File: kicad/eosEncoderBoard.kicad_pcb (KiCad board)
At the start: 2 copper layers, 235 x 45 mm, 72 parts, among them J1 USB_C_Receptacle_USB2.0_16P, J2 DEBUG, J3 EXTRA, SW1 RotaryEncoder, SW10 SHUTTER, SW11 SW_Push, SW2 RotaryEncoder, SW3 RotaryEncoder, SW4 RotaryEncoder, SW5 INTENS, SW6 FORM, SW7 FOCUS, SW8 IMAGE, SW9 COLOR, U1 STM32L072CZT6TR, U2 PCA9548ADB, U3 TPS62A01DRLR, Y1 OSC16M-3.3I/S3T

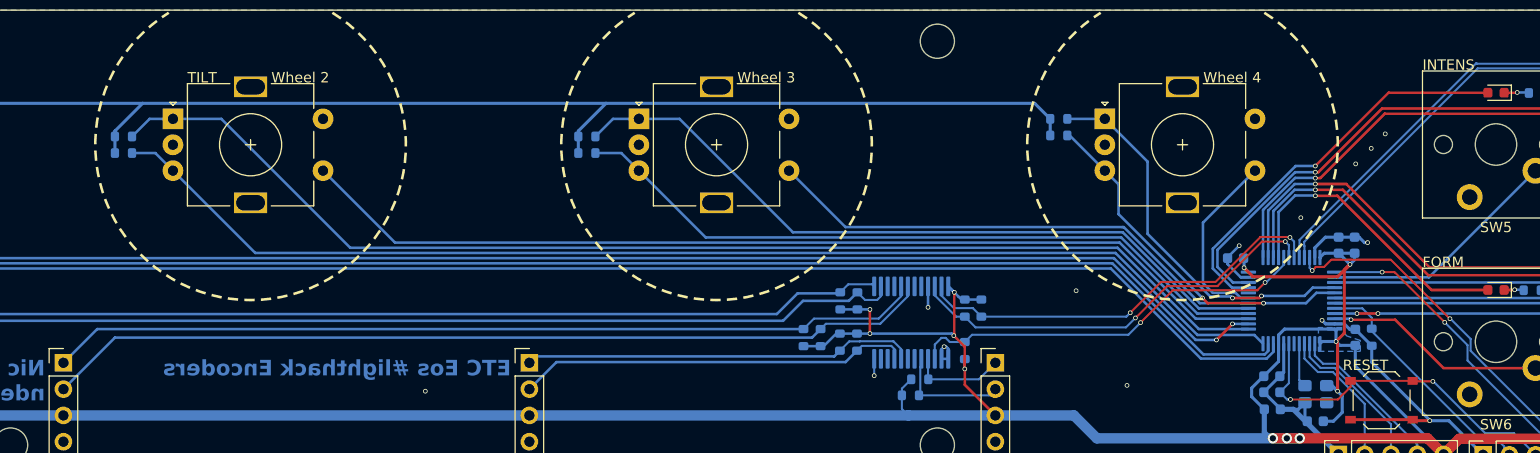
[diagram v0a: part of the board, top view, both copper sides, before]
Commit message: some minor include optimizations, going to stick with adafruit display library
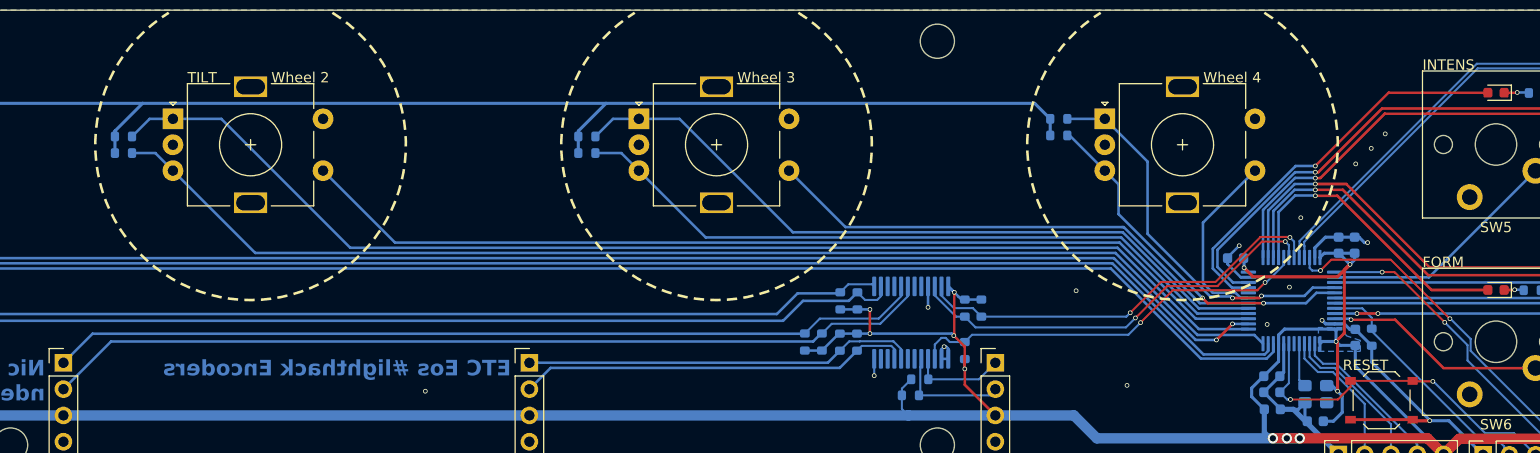
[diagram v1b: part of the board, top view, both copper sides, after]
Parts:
- moved R15 0.44 mm to (152.8, 82.0)
- moved R16 0.44 mm to (151.2, 82.0)
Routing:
- net +3.3V: track 552.9 -> 553.6 mm
- net GND: vias 22 -> 24
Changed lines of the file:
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@@
 	(footprint "Resistor_SMD:R_0603_1608Metric"
 		(layer "B.Cu")
-		(at 151.0725 81.625 90)
+		(at 151.2 82.05 90)
 		(descr "Resistor SMD 0603 (1608 Metric), square (rectangular) end terminal, IPC-7351 nominal, (Body size source: IPC-SM-782 page 72, https://www.pcb-3d.com/wordpress/wp-content/uploads/ipc-sm-782a_amendment_1_and_2.pdf)")
 		(tags "resistor")
@@
 	(footprint "Resistor_SMD:R_0603_1608Metric"
 		(layer "B.Cu")
-		(at 152.7225 81.625 90)
+		(at 152.85 82.05 90)
 		(descr "Resistor SMD 0603 (1608 Metric), square (rectangular) end terminal, IPC-7351 nominal, (Body size source: IPC-SM-782 page 72, https://www.pcb-3d.com/wordpress/wp-content/uploads/ipc-sm-782a_amendment_1_and_2.pdf)")
 		(tags "resistor")
@@
 	)
 	(segment
+		(start 154.4875 81.2375)
+		(end 152.85 82.875)
+		(width 0.25)
+		(layer "B.Cu")
+		(net "+3.3V")
+	)
+	(segment
 		(start 165.0625 76.675)
 		(end 165.05 76.675)
@@
 	)
 	(segment
+		(start 154.5875 81.2375)
+		(end 154.4875 81.2375)
+		(width 0.25)
+		(layer "B.Cu")
+		(net "+3.3V")
+	)
+	(segment
 		(start 248.104106 82.55)
 		(end 258.267202 72.386904)
@@
 	)
 	(segment
+		(start 152.85 82.875)
+		(end 151.2 82.875)
+		(width 0.25)
+		(layer "B.Cu")
+		(net "+3.3V")
+	)
+	(segment
 		(start 160.575 86.55)
 		(end 161.475 85.65)
@@
 	)
 	(segment
-		(start 156.2375 81.2375)
-		(end 154.5875 81.2375)
-		(width 0.25)
-		(layer "B.Cu")
-		(net "+3.3V")
-	)
-	(segment
 		(start 202.1125 86.2625)
 		(end 203.1 87.25)
@@
 	)
 	(segment
-		(start 152.7225 82.45)
-		(end 151.0725 82.45)
-		(width 0.25)
-		(layer "B.Cu")
-		(net "+3.3V")
-	)
-	(segment
 		(start 195.5 85.35)
 		(end 194.35 86.5)
@@
 	)
 	(segment
+		(start 156.2375 81.2375)
+		(end 154.5875 81.2375)
+		(width 0.25)
+		(layer "B.Cu")
+		(net "+3.3V")
+	)
+	(segment
 		(start 260.392202 72.042202)
 		(end 259.85 71.5)
@@
 	)
 	(segment
-		(start 154.2375 81.2375)
-		(end 153.025 82.45)
-		(width 0.25)
-		(layer "B.Cu")
-		(net "+3.3V")
-	)
-	(segment
 		(start 84.575 61.675)
 		(end 87.25 59)
@@
 	)
 	(via
+		(at 195.85 80.35)
+		(size 0.45)
+		(drill 0.3)
+		(layers "F.Cu" "B.Cu")
+		(net "GND")
+	)
+	(via
 		(at 199.1 70.05)
 		(size 0.45)
@@
 	)
 	(via
+		(at 198 76.75)
+		(size 0.45)
+		(drill 0.3)
+		(layers "F.Cu" "B.Cu")
+		(net "GND")
+	)
+	(via
 		(at 261.417202 69.461904)
 		(size 0.45)
@@
 	)
 	(segment
-		(start 160.5 77.624999)
-		(end 158.337499 79.7875)
-		(width 0.2)
+		(start 151.175 81.25)
+		(end 151.2 81.225)
+		(width 0.25)
 		(layer "B.Cu")
 		(net "SDA2")
 	)
 	(segment
-		(start 160.5 76.675)
-		(end 160.5 77.624999)
+		(start 158.337499 79.7875)
+		(end 152.65 79.7875)
 		(width 0.2)
 		(layer "B.Cu")
@@
 	)
 	(segment
-		(start 82.86 80.8)
-		(end 151.0725 80.8)
+		(start 82.41 81.25)
+		(end 151.175 81.25)
 		(width 0.25)
 		(layer "B.Cu")
@@
 	)
 	(segment
-		(start 152.085 79.7875)
-		(end 151.0725 80.8)
+		(start 160.5 77.624999)
+		(end 158.337499 79.7875)
 		(width 0.2)
 		(layer "B.Cu")
@@
 	)
 	(segment
-		(start 158.337499 79.7875)
-		(end 152.085 79.7875)
+		(start 151.2 81.225)
+		(end 151.2125 81.225)
 		(width 0.2)
 		(layer "B.Cu")
@@
 	(segment
 		(start 79.6 84.06)
-		(end 82.86 80.8)
+		(end 82.41 81.25)
 		(width 0.25)
 		(layer "B.Cu")
@@
 	)
 	(segment
-		(start 158.487499 80.2875)
-		(end 153.235 80.2875)
+		(start 160.5 76.675)
+		(end 160.5 77.624999)
+		(width 0.2)
+		(layer "B.Cu")
+		(net "SDA2")
+	)
+	(segment
+		(start 151.2125 81.225)
+		(end 152.65 79.7875)
 		(width 0.2)
 		(layer "B.Cu")
+		(net "SDA2")
+	)
+	(segment
+		(start 152.775 81.225)
+		(end 152.85 81.225)
+		(width 0.25)
+		(layer "B.Cu")
 		(net "SCL2")
 	)
@@
 	)
 	(segment
-		(start 151.8975 81.625)
-		(end 84.575 81.625)
+		(start 84.2 82)
+		(end 152 82)
 		(width 0.25)
 		(layer "B.Cu")
@@
 	)
 	(segment
-		(start 152.7225 80.8)
-		(end 151.8975 81.625)
+		(start 152.8625 81.225)
+		(end 153.8 80.2875)
+		(width 0.2)
+		(layer "B.Cu")
+		(net "SCL2")
+	)
+	(segment
+		(start 79.6 86.6)
+		(end 84.2 82)
 		(width 0.25)
 		(layer "B.Cu")
@@
 	)
 	(segment
-		(start 153.235 80.2875)
-		(end 152.7225 80.8)
+		(start 152.85 81.225)
+		(end 152.8625 81.225)
 		(width 0.2)
 		(layer "B.Cu")
@@
 	)
 	(segment
-		(start 84.575 81.625)
-		(end 79.6 86.6)
+		(start 152 82)
+		(end 152.775 81.225)
 		(width 0.25)
 		(layer "B.Cu")
@@
 	)
 	(segment
+		(start 158.487499 80.2875)
+		(end 153.8 80.2875)
+		(width 0.2)
+		(layer "B.Cu")
+		(net "SCL2")
+	)
+	(segment
 		(start 154.5225 77.35)
 		(end 154.6225 77.25)
@@
 	)
 	(segment
+		(start 154.5875 82.8875)
+		(end 153.425 84.05)
+		(width 0.25)
+		(layer "B.Cu")
+		(net "SDA3")
+	)
+	(segment
 		(start 156.501104 81.9875)
 		(end 155.4875 81.9875)
@@
 	)
 	(segment
-		(start 155.4875 81.9875)
-		(end 154.5875 82.8875)
-		(width 0.2)
+		(start 124.61 84.05)
+		(end 124.6 84.06)
+		(width 0.25)
 		(layer "B.Cu")
 		(net "SDA3")
 	)
 	(segment
-		(start 125.2225 83.4375)
-		(end 124.6 84.06)
-		(width 0.25)
+		(start 155.4875 81.9875)
+		(end 154.5875 82.8875)
+		(width 0.2)
 		(layer "B.Cu")
 		(net "SDA3")
@@
 	)
 	(segment
-		(start 154.5875 82.8875)
-		(end 154.0375 83.4375)
-		(width 0.25)
-		(layer "B.Cu")
-		(net "SDA3")
-	)
-	(segment
-		(start 154.0375 83.4375)
-		(end 125.2225 83.4375)
+		(start 153.425 84.05)
+		(end 124.61 84.05)
 		(width 0.25)
 		(layer "B.Cu")
@@
 	(segment
 		(start 156.2375 82.8875)
-		(end 155.1375 83.9875)
+		(end 154.575 84.55)
 		(width 0.25)
 		(layer "B.Cu")
@@
 	)
 	(segment
-		(start 127.2125 83.9875)
-		(end 124.6 86.6)
-		(width 0.25)
+		(start 159.85 82.725001)
+		(end 159.549999 82.425)
+		(width 0.2)
 		(layer "B.Cu")
 		(net "SCL3")
 	)
 	(segment
-		(start 159.85 82.725001)
-		(end 159.549999 82.425)
-		(width 0.2)
+		(start 126.65 84.55)
+		(end 124.6 86.6)
+		(width 0.25)
 		(layer "B.Cu")
 		(net "SCL3")
 	)
 	(segment
-		(start 155.1375 83.9875)
-		(end 127.2125 83.9875)
+		(start 154.575 84.55)
+		(end 126.65 84.55)
 		(width 0.25)
 		(layer "B.Cu")
@@
 	)
 	(segment
-		(start 201.35 74.8)
+		(start 201 75.15)
 		(end 202.0444 74.1056)
 		(width 0.2)
@@
 	)
 	(segment
-		(start 200.2 75.15)
-		(end 200.55 74.8)
-		(width 0.2)
-		(layer "F.Cu")
-		(net "SWDIO")
-	)
-	(segment
 		(start 202.0444 74.1056)
 		(end 207.8056 74.1056)
@@
 		(net "SWDIO")
 	)
-	(segment
-		(start 200.55 74.8)
-		(end 201.35 74.8)
-		(width 0.2)
-		(layer "F.Cu")
-		(net "SWDIO")
-	)
 	(via
-		(at 200.2 75.15)
+		(at 201 75.15)
 		(size 0.45)
 		(drill 0.3)
@@
 	)
 	(segment
+		(start 199.95 74.9)
+		(end 199.95 73.8875)
+		(width 0.2)
+		(layer "B.Cu")
+		(net "SWDIO")
+	)
+	(segment
 		(start 215.5 81.75)
 		(end 215.5 82.9)
@@
 	)
 	(segment
-		(start 199.95 74.9)
+		(start 201 75.15)
 		(end 200.2 75.15)
 		(width 0.2)
@@
 	)
 	(segment
-		(start 215.5 82.9)
-		(end 223.25 90.65)
+		(start 200.2 75.15)
+		(end 199.95 74.9)
 		(width 0.2)
 		(layer "B.Cu")
@@
 	)
 	(segment
-		(start 213.5 79.8)
-		(end 213.55 79.8)
+		(start 215.5 82.9)
+		(end 223.25 90.65)
 		(width 0.2)
 		(layer "B.Cu")
@@
 	)
 	(segment
-		(start 199.95 73.8875)
-		(end 199.95 74.9)
+		(start 213.5 79.8)
+		(end 213.55 79.8)
 		(width 0.2)
 		(layer "B.Cu")
@@
 	)
 	(segment
-		(start 198.95 73.8875)
-		(end 198.95 72.781249)
-		(width 0.2)
-		(layer "B.Cu")
-		(net "D-")
-	)
-	(segment
 		(start 198.975 72.756249)
-		(end 198.975 72.188606)
-		(width 0.2)
-		(layer "B.Cu")
-		(net "D-")
-	)
-	(segment
-		(start 198.95 72.781249)
-		(end 198.975 72.756249)
-		(width 0.2)
-		(layer "B.Cu")
-		(net "D-")
-	)
-	(segment
-		(start 216.043606 55.12)
-		(end 216.098605 55.174999)
+		(end 198.975 72.298604)
 		(width 0.2)
 		(layer "B.Cu")
@@
 	)
 	(segment
-		(start 198.975 72.188606)
-		(end 216.043606 55.12)
+		(start 198.975 72.298604)
+		(end 216.098605 55.174999)
 		(width 0.2)
 		(layer "B.Cu")
@@
 		(width 0.2)
 		(layer "B.Cu")
+		(net "D-")
+	)
+	(segment
+		(start 198.95 72.781249)
+		(end 198.975 72.756249)
+		(width 0.2)
+		(layer "B.Cu")
+		(net "D-")
+	)
+	(segment
+		(start 198.95 73.8875)
+		(end 198.95 72.781249)
+		(width 0.2)
+		(layer "B.Cu")

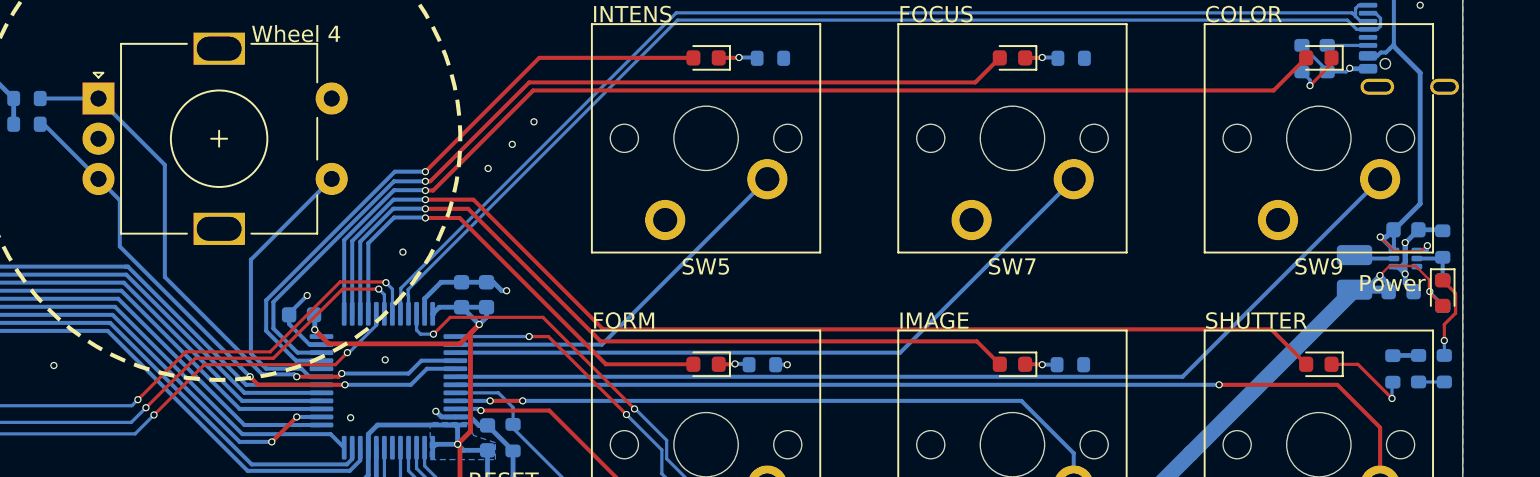
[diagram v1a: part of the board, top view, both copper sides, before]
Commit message: move power LED to be on the MCU
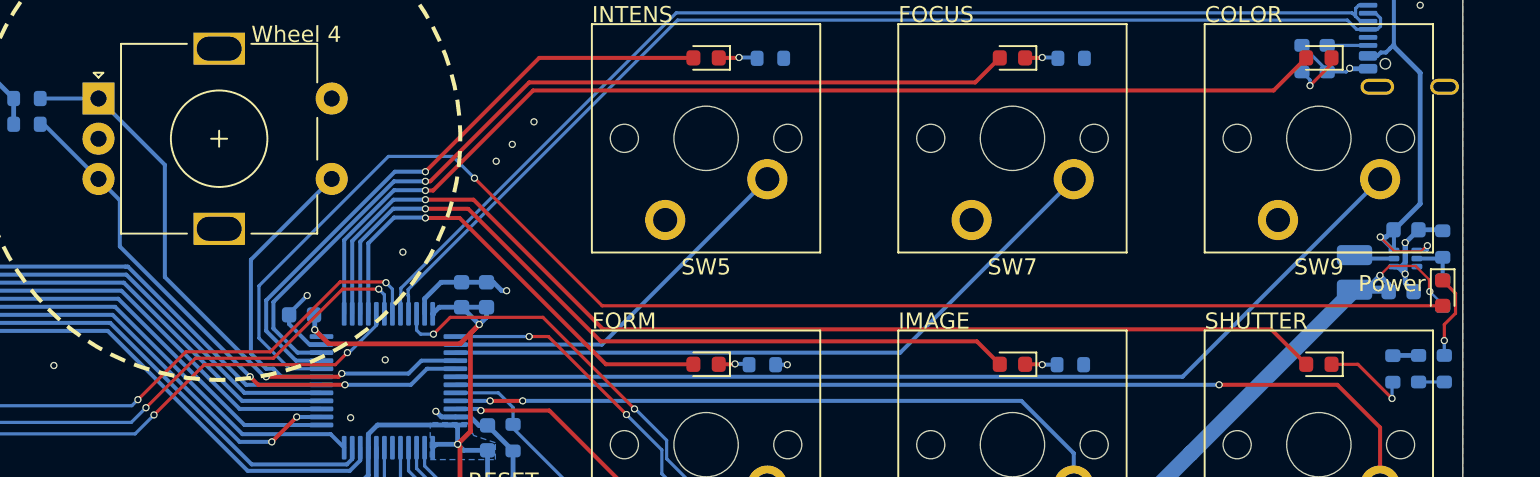
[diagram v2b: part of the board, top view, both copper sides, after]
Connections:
- D7 pad 2: +3.3V -> LED
- U1 pad 20: unconnected-(U1-PB2-Pad20) -> LED
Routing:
- net LED: track 0.00 -> 88.7 mm, vias 0 -> 1
- net +3.3V: track 553.6 -> 552.4 mm

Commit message: ordered
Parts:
- added C11: 0.1u, Capacitor_SMD:C_0603_1608Metric, B.Cu at (168.4, 76.4)
- added D8: 4A, Diode_SMD:D_SOD-923, B.Cu at (263.3, 62.6)
- added U4: USBLC6-2SC6, Package_TO_SOT_SMD:SOT-23-6, B.Cu at (251.9, 55.4)
- moved R6 4.29 mm to (177.0, 66.2)
- moved R8 4.29 mm to (177.0, 64.6)
- moved R1 2.90 mm to (42.0, 66.2)
- moved R2 2.90 mm to (42.0, 64.6)
- moved R3 2.88 mm to (87.0, 66.2)
- moved R4 2.88 mm to (87.0, 64.6)
- moved R5 2.75 mm to (131.8, 66.0)
- moved R7 2.75 mm to (131.8, 64.4)
- moved SW1 2.50 mm to (45.2, 63.0)
- moved SW2 2.50 mm to (90.2, 63.0)
- moved SW3 2.50 mm to (135.2, 63.0)
- moved SW4 2.50 mm to (180.2, 63.0)
- moved DP1 1.87 mm to (36.0, 85.2)
- moved DP2 1.87 mm to (81.0, 85.2)
- moved DP3 1.87 mm to (126.0, 85.2)
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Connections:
- J1 pad A4: +5V -> VBUS
- J1 pad A6: D+ -> /USB_D+
- J1 pad A7: D- -> /USB_D-
- J1 pad A9: +5V -> VBUS
- J1 pad B4: +5V -> VBUS
- J1 pad B6: D+ -> /USB_D+
- J1 pad B7: D- -> /USB_D-
- J1 pad B9: +5V -> VBUS
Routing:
- net VBUS: track 0.00 -> 23.1 mm
- net +5V: track 27.7 -> 14.6 mm
- net D+: track 70.6 -> 60.1 mm
- net D-: track 70.4 -> 60.8 mm
- net /USB_D+: track 0.00 -> 8.91 mm
- net +3.3V: track 552.4 -> 560.9 mm
- net /USB_D-: track 0.00 -> 7.98 mm
- net GND: track 103.6 -> 109.8 mm, vias 24 -> 25
- net B4: track 34.6 -> 30.2 mm
- net LED_IMAGE: track 49.1 -> 45.1 mm
- net LED_SHUTTER: track 69.1 -> 65.1 mm
- net LED_FORM: track 29.0 -> 25.0 mm
- net LED: track 88.7 -> 85.3 mm
- net A4: track 37.5 -> 34.4 mm
- net A3: track 71.3 -> 68.5 mm
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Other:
- board size 235 x 45 mm -> 235.7 x 45.7 mm
- board text added: "ETC Eos #lighthack Encoders #knobOS"
- board text removed: "ETC Eos #lighthack Encoders"
